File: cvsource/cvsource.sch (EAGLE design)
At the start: 105 parts, among them IC1 OPA4130P, IC2 OPA2134P, IC3 78L05Z, P1 US-EVUF3J, P2 US-EVUF3J, P3 US-EVUF3J, P4 US-EVUF3J, X1 2516-

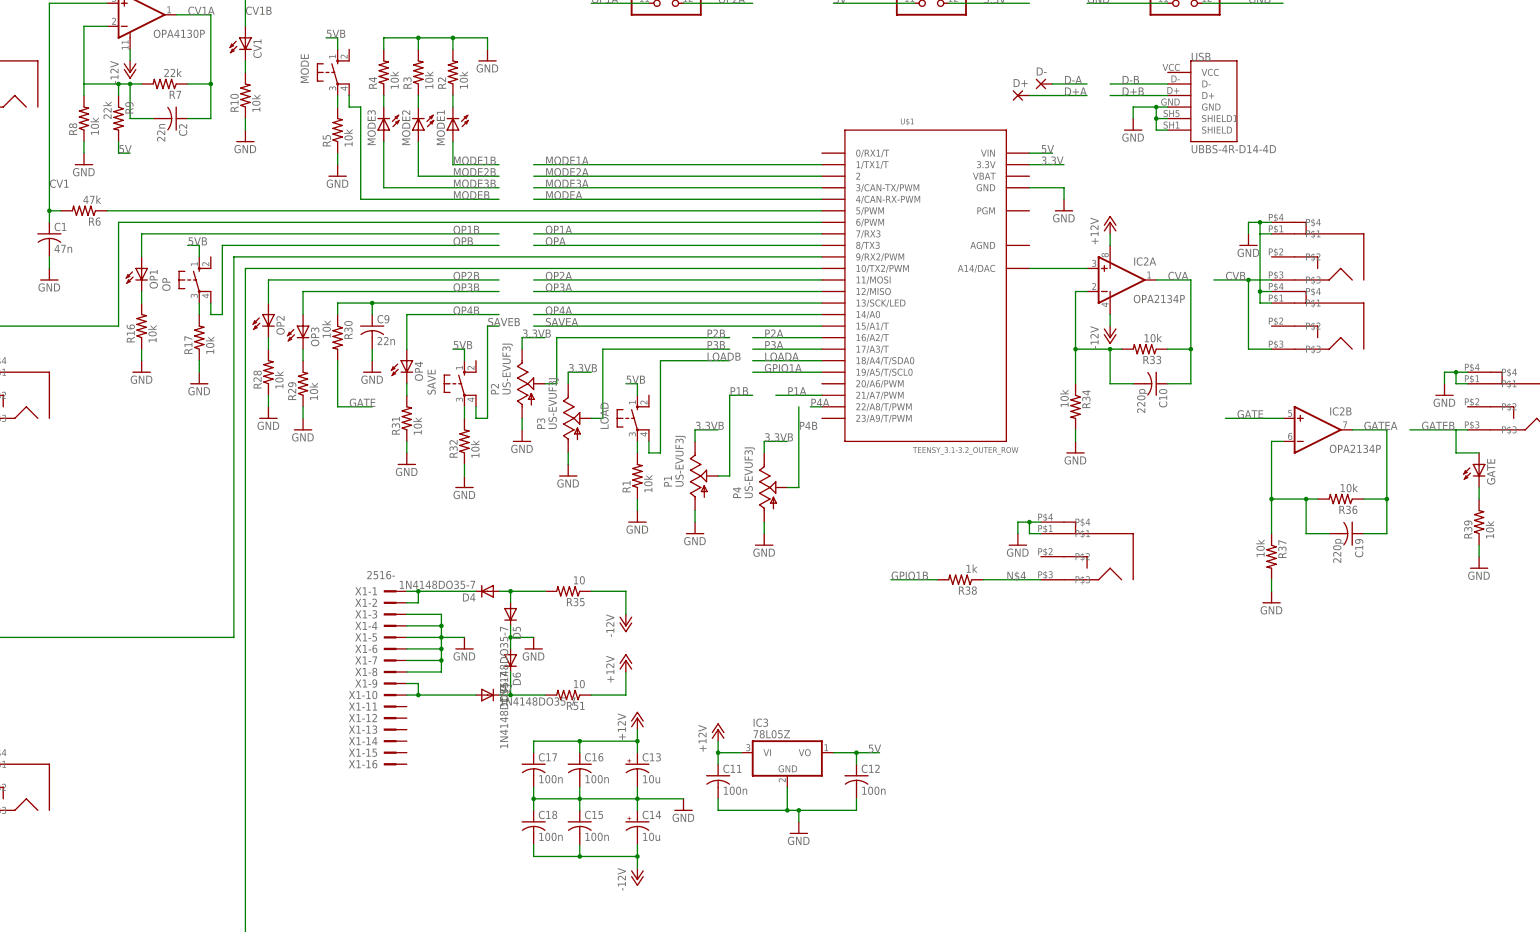
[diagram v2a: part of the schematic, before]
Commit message: more work on cvsource and added zipped code
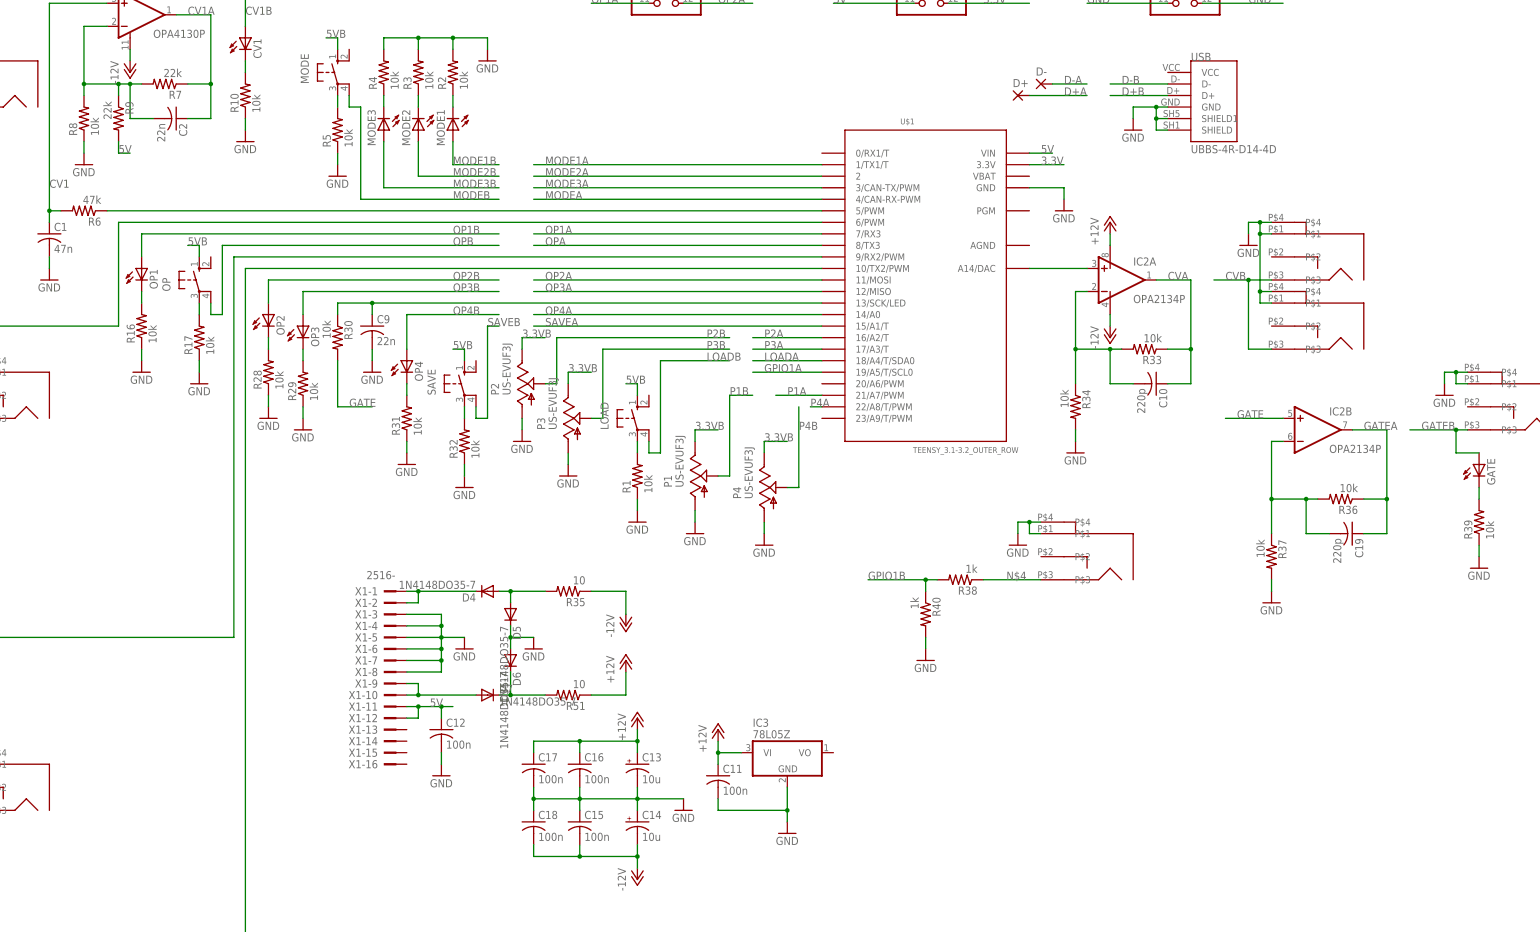
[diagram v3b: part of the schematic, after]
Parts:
- added R40: 1k, dan:R-US_0207/2V
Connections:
- net 5V: now also X1-11.KL, X1-12.KL; no longer IC3.VO
- net GND: now also R40.2
- net GPIO1B: now also R40.1
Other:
- moved on the sheet: C12
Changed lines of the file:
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@@
 <part name="R39" library="dan" deviceset="R-US_" device="0207/2V" value="10k"/>
 <part name="GND42" library="dan" deviceset="GND" device=""/>
+<part name="R40" library="dan" deviceset="R-US_" device="0207/2V" value="1k"/>
+<part name="GND43" library="dan" deviceset="GND" device=""/>
+<part name="GND44" library="dan" deviceset="GND" device=""/>
 </parts>
 <sheets>
@@
 <instance part="P+3" gate="1" x="10.16" y="-48.26"/>
 <instance part="C11" gate="G$1" x="10.16" y="-58.42"/>
-<instance part="C12" gate="G$1" x="40.64" y="-58.42"/>
-<instance part="GND34" gate="1" x="27.94" y="-71.12"/>
+<instance part="C12" gate="G$1" x="-50.8" y="-48.26"/>
+<instance part="GND34" gate="1" x="25.4" y="-71.12"/>
 <instance part="P+4" gate="1" x="-7.62" y="-45.72"/>
 <instance part="P-3" gate="1" x="-7.62" y="-81.28"/>
@@
 <instance part="R39" gate="G$1" x="177.8" y="-2.54" rot="R90"/>
 <instance part="GND42" gate="1" x="177.8" y="-12.7"/>
+<instance part="R40" gate="G$1" x="55.88" y="-22.86" rot="R270"/>
+<instance part="GND43" gate="1" x="55.88" y="-33.02"/>
+<instance part="GND44" gate="1" x="-50.8" y="-58.42"/>
 </instances>
 <busses>
@@
 <wire x1="129.54" y1="60.96" x2="129.54" y2="48.26" width="0.1524" layer="91"/>
 <junction x="129.54" y="48.26"/>
+<junction x="129.54" y="60.96"/>
 </segment>
 <segment>
 <pinref part="GND34" gate="1" pin="GND"/>
-<wire x1="27.94" y1="-68.58" x2="27.94" y2="-66.04" width="0.1524" layer="91"/>
+<wire x1="25.4" y1="-68.58" x2="25.4" y2="-66.04" width="0.1524" layer="91"/>
 <pinref part="C11" gate="G$1" pin="2"/>
 <wire x1="10.16" y1="-63.5" x2="10.16" y2="-66.04" width="0.1524" layer="91"/>
-<pinref part="C12" gate="G$1" pin="2"/>
 <wire x1="10.16" y1="-66.04" x2="25.4" y2="-66.04" width="0.1524" layer="91"/>
-<wire x1="25.4" y1="-66.04" x2="27.94" y2="-66.04" width="0.1524" layer="91"/>
-<wire x1="27.94" y1="-66.04" x2="40.64" y2="-66.04" width="0.1524" layer="91"/>
-<wire x1="40.64" y1="-66.04" x2="40.64" y2="-63.5" width="0.1524" layer="91"/>
 <pinref part="IC3" gate="A1" pin="GND"/>
 <wire x1="25.4" y1="-60.96" x2="25.4" y2="-66.04" width="0.1524" layer="91"/>
 <junction x="25.4" y="-66.04"/>
-<junction x="27.94" y="-66.04"/>
 </segment>
 <segment>
@@
 <wire x1="177.8" y1="-10.16" x2="177.8" y2="-7.62" width="0.1524" layer="91"/>
 </segment>
+<segment>
+<pinref part="R40" gate="G$1" pin="2"/>
+<pinref part="GND43" gate="1" pin="GND"/>
+<wire x1="55.88" y1="-30.48" x2="55.88" y2="-27.94" width="0.1524" layer="91"/>
+</segment>
+<segment>
+<pinref part="GND44" gate="1" pin="GND"/>
+<pinref part="C12" gate="G$1" pin="2"/>
+<wire x1="-50.8" y1="-55.88" x2="-50.8" y2="-53.34" width="0.1524" layer="91"/>
+</segment>
 </net>
 <net name="N$1" class="0">
@@
 </segment>
 <segment>
-<pinref part="C12" gate="G$1" pin="1"/>
-<wire x1="40.64" y1="-55.88" x2="40.64" y2="-53.34" width="0.1524" layer="91"/>
-<pinref part="IC3" gate="A1" pin="VO"/>
-<wire x1="40.64" y1="-53.34" x2="35.56" y2="-53.34" width="0.1524" layer="91"/>
-<wire x1="40.64" y1="-53.34" x2="45.72" y2="-53.34" width="0.1524" layer="91"/>
-<junction x="40.64" y="-53.34"/>
-<label x="43.18" y="-53.34" size="1.778" layer="95"/>
-</segment>
-<segment>
 <pinref part="JP4" gate="A" pin="11"/>
 <wire x1="53.34" y1="111.76" x2="35.56" y2="111.76" width="0.1524" layer="91"/>
 <label x="35.56" y="111.76" size="1.778" layer="95"/>
+</segment>
+<segment>
+<pinref part="X1" gate="-11" pin="KL"/>
+<wire x1="-58.42" y1="-43.18" x2="-55.88" y2="-43.18" width="0.1524" layer="91"/>
+<wire x1="-55.88" y1="-43.18" x2="-55.88" y2="-45.72" width="0.1524" layer="91"/>
+<pinref part="X1" gate="-12" pin="KL"/>
+<wire x1="-55.88" y1="-45.72" x2="-58.42" y2="-45.72" width="0.1524" layer="91"/>
+<wire x1="-55.88" y1="-43.18" x2="-50.8" y2="-43.18" width="0.1524" layer="91"/>
+<junction x="-55.88" y="-43.18"/>
+<label x="-53.34" y="-43.18" size="1.778" layer="95"/>
+<pinref part="C12" gate="G$1" pin="1"/>
+<wire x1="-50.8" y1="-43.18" x2="-48.26" y2="-43.18" width="0.1524" layer="91"/>
+<wire x1="-50.8" y1="-45.72" x2="-50.8" y2="-43.18" width="0.1524" layer="91"/>
+<junction x="-50.8" y="-43.18"/>
 </segment>
 </net>
@@
 <pinref part="R8" gate="G$1" pin="2"/>
 <wire x1="-129.54" y1="91.44" x2="-129.54" y2="93.98" width="0.1524" layer="91"/>
+<junction x="-129.54" y="93.98"/>
 </segment>
 </net>
@@
 <wire x1="177.8" y1="12.7" x2="172.72" y2="12.7" width="0.1524" layer="91"/>
 <wire x1="172.72" y1="12.7" x2="172.72" y2="17.78" width="0.1524" layer="91"/>
+<junction x="172.72" y="17.78"/>
 </segment>
 <segment>
@@
 <segment>
 <pinref part="R38" gate="G$1" pin="2"/>
-<wire x1="58.42" y1="-15.24" x2="48.26" y2="-15.24" width="0.1524" layer="91"/>
-<label x="48.26" y="-15.24" size="1.778" layer="95"/>
+<wire x1="58.42" y1="-15.24" x2="55.88" y2="-15.24" width="0.1524" layer="91"/>
+<label x="43.18" y="-15.24" size="1.778" layer="95"/>
+<pinref part="R40" gate="G$1" pin="1"/>
+<wire x1="55.88" y1="-15.24" x2="43.18" y2="-15.24" width="0.1524" layer="91"/>
+<wire x1="55.88" y1="-17.78" x2="55.88" y2="-15.24" width="0.1524" layer="91"/>
+<junction x="55.88" y="-15.24"/>
 </segment>
 </net>
@@
 <pinref part="R38" gate="G$1" pin="1"/>
 <pinref part="CVOUT7" gate="G$1" pin="P$3"/>
+<label x="73.66" y="-15.24" size="1.778" layer="95"/>
 <wire x1="68.58" y1="-15.24" x2="81.28" y2="-15.24" width="0.1524" layer="91"/>
-<label x="73.66" y="-15.24" size="1.778" layer="95"/>
 </segment>
 </net>
@@
 </sheet>
 </sheets>
+<errors>
+</errors>
 </schematic>
 </drawing>

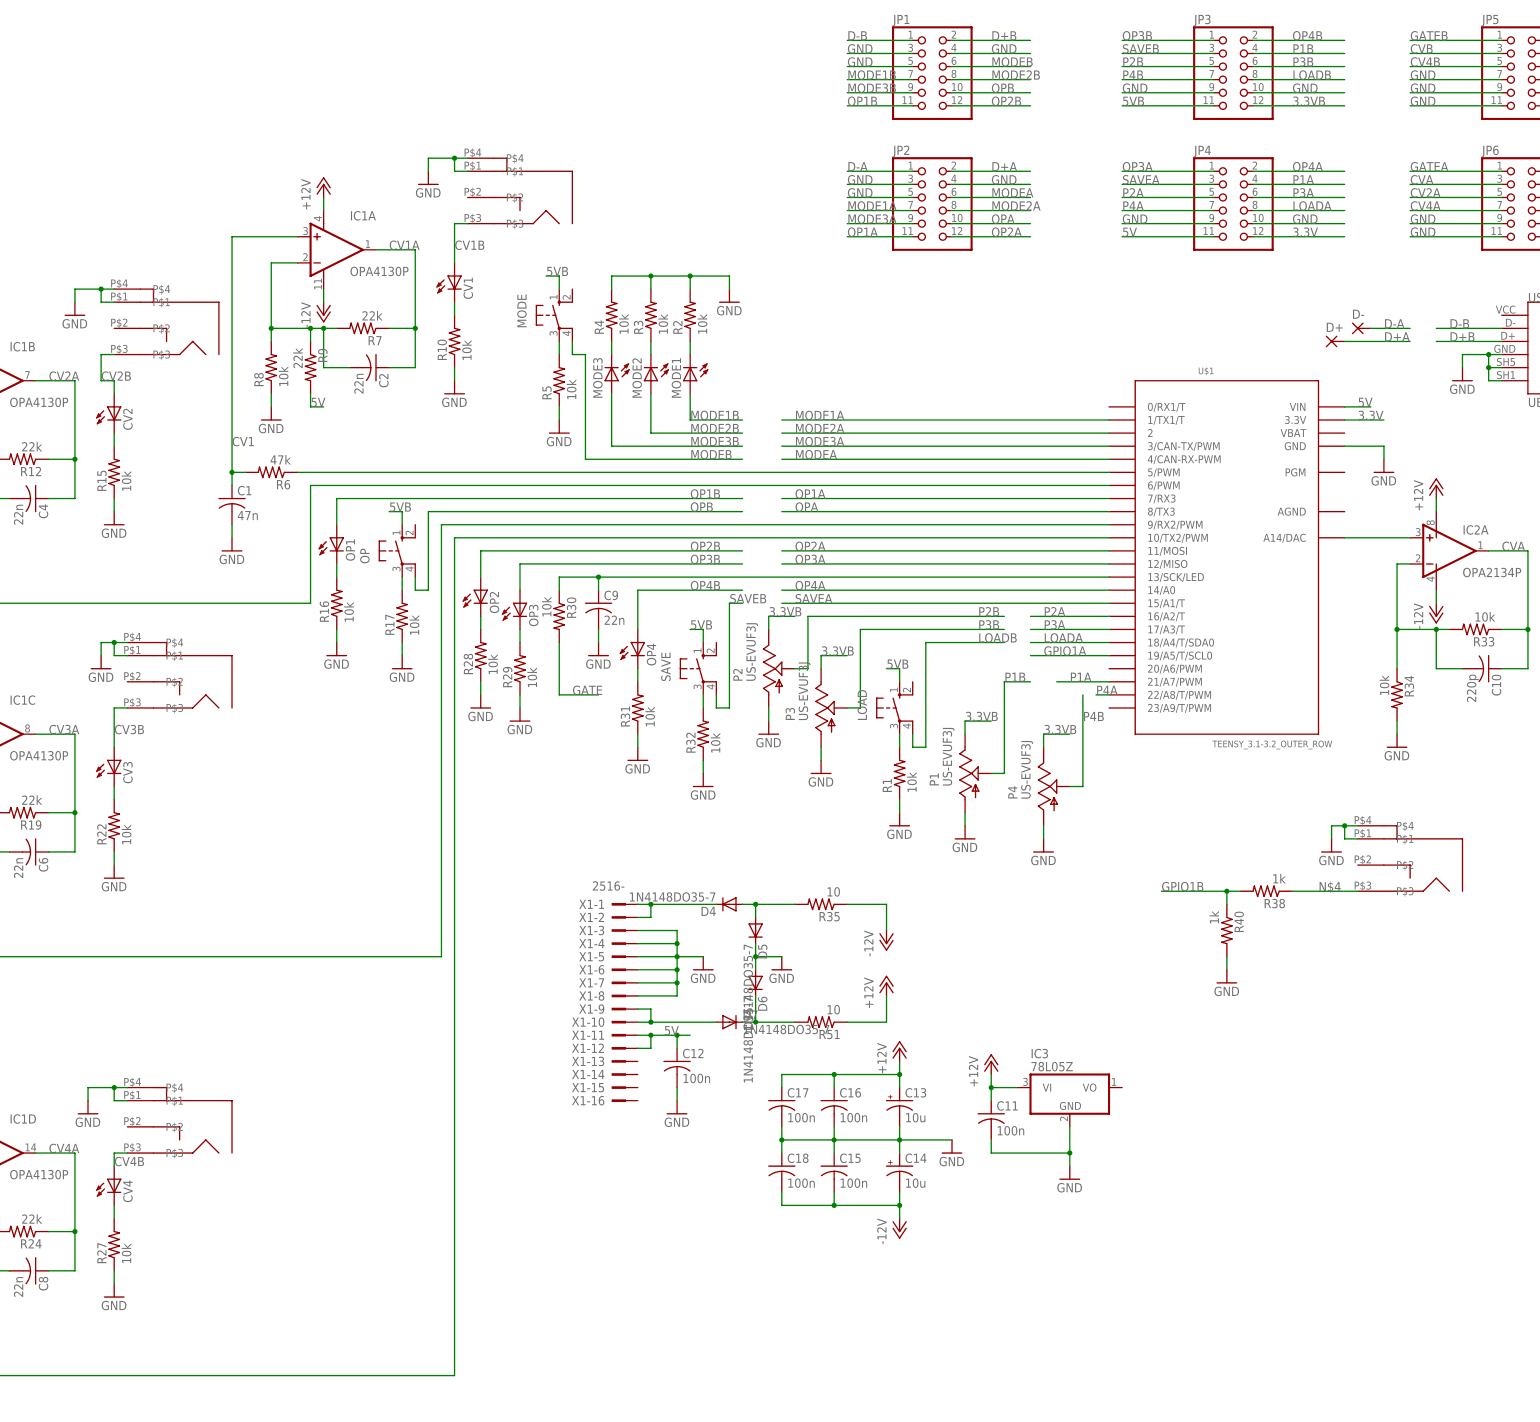
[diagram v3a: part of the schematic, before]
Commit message: added tri and linear mod to vco, fixed serious errors with cvsource
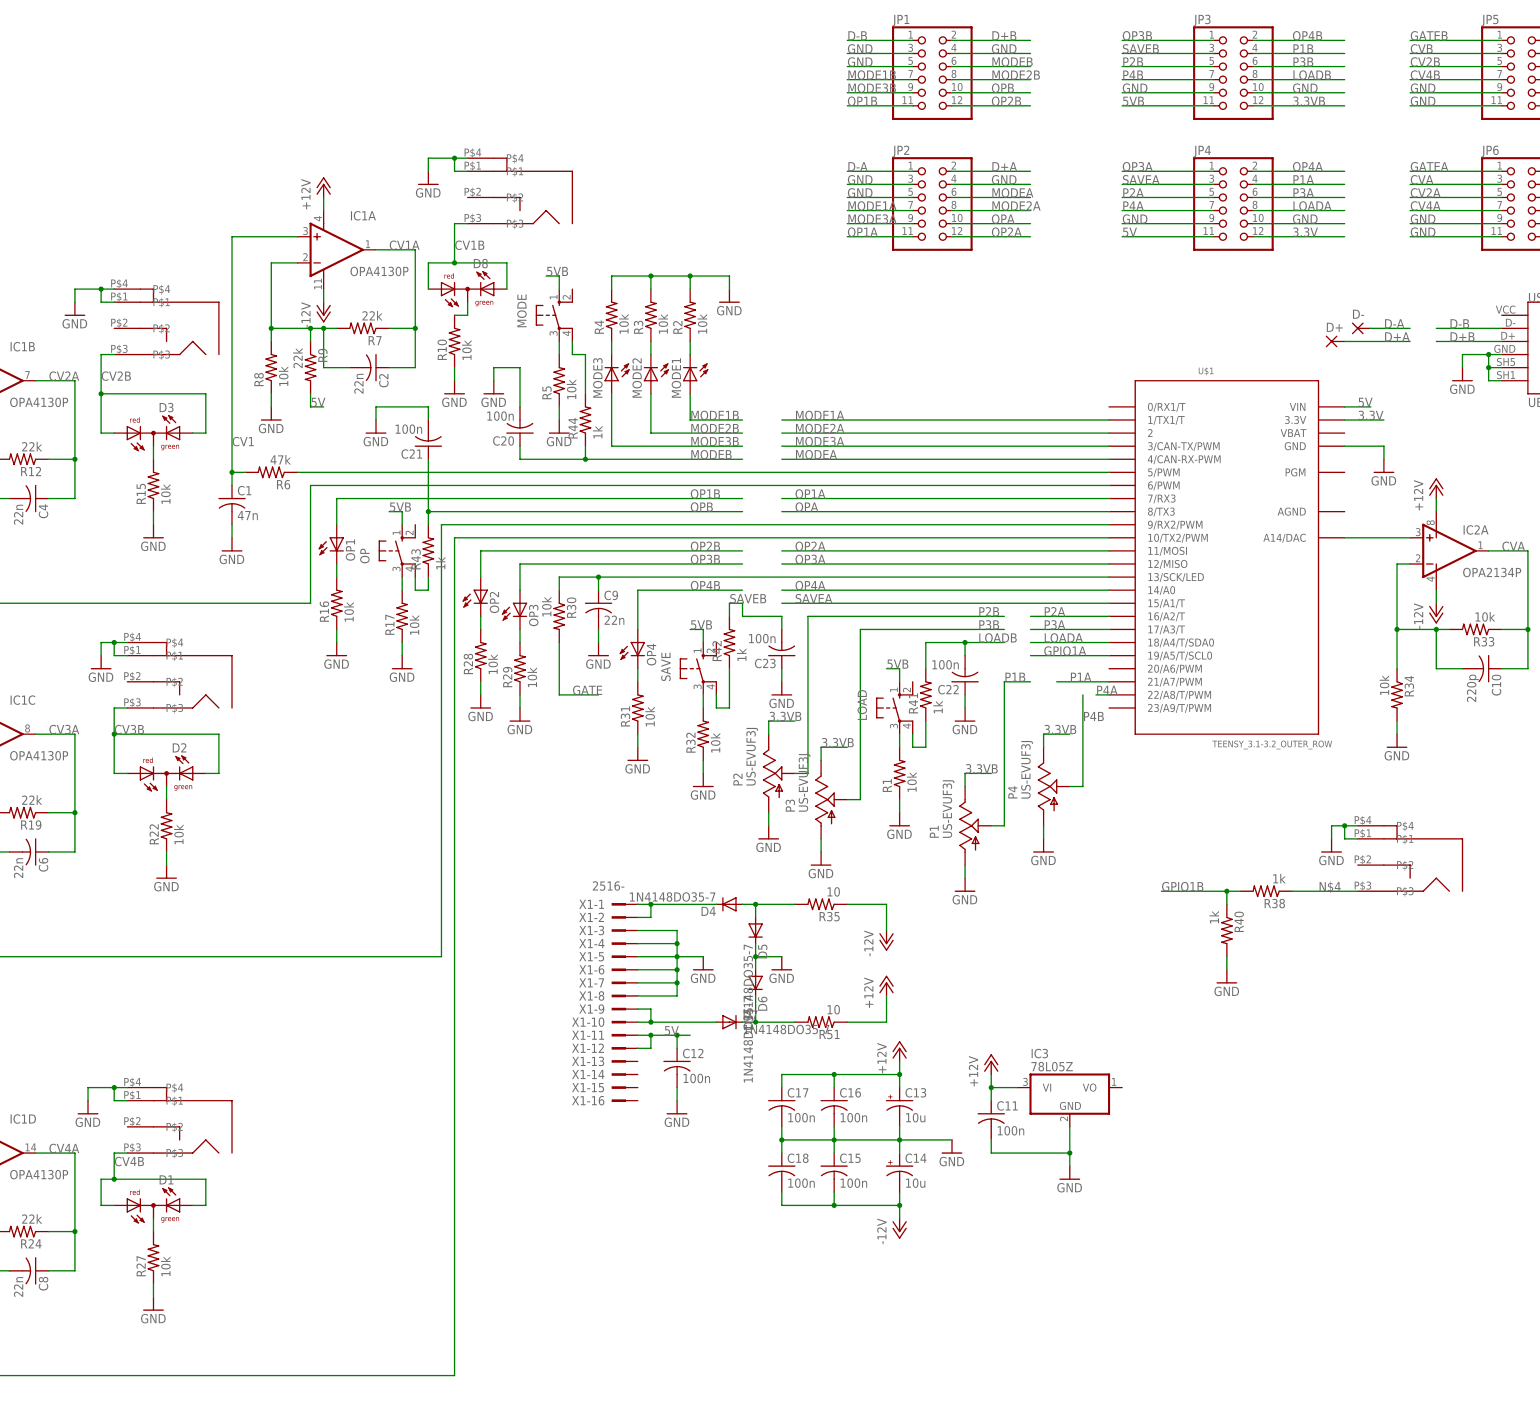
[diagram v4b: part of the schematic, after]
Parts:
- removed CV1, CV2, CV3, CV4: (no value), dan:LED5MM
- added C20, C21, C22, C23: 100n, dan:C-US075-032X103
- added D1, D2, D3, D8: (no value), dan:DUOLED5MM
- added R41, R42, R43, R44: 1k, dan:R-US_0207/2V
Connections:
- removed net N$29: CV4.C, R27.2
- new net N$12: R42.1, SAVE.P1
- new net N$16: OP.P1, R43.1
- new net N$18: MODE.P1, R44.2
- new net N$19: D1.C, R27.2
- new net N$7: LOAD.P1, R41.1
- net CV1B: now also D8.AG, D8.AR; no longer CV1.A
- net CV2B: now also D3.AG, D3.AR, JP5.5; no longer CV2.A
- net CV3B: now also D2.AG, D2.AR; no longer CV3.A
- net CV4B: now also D1.AG, D1.AR, JP5.7; no longer CV4.A, JP5.5
- net GND: now also C20.2, C21.2, C22.1, C23.1; no longer JP5.7
- net LOADB: now also C22.2, R41.2; no longer LOAD.P1
- net MODEB: now also C20.1, R44.1; no longer MODE.P1
- net N$13: now also D8.C; no longer CV1.C
- net N$17: now also D3.C; no longer CV2.C
- net N$24: now also D2.C; no longer CV3.C
- net OPB: now also C21.1, R43.2; no longer OP.P1
- net SAVEB: now also C23.2, R42.2; no longer SAVE.P1
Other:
- moved on the sheet: P1, P2, P3, R15, R22, R27
